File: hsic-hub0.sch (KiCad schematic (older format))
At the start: 17 parts

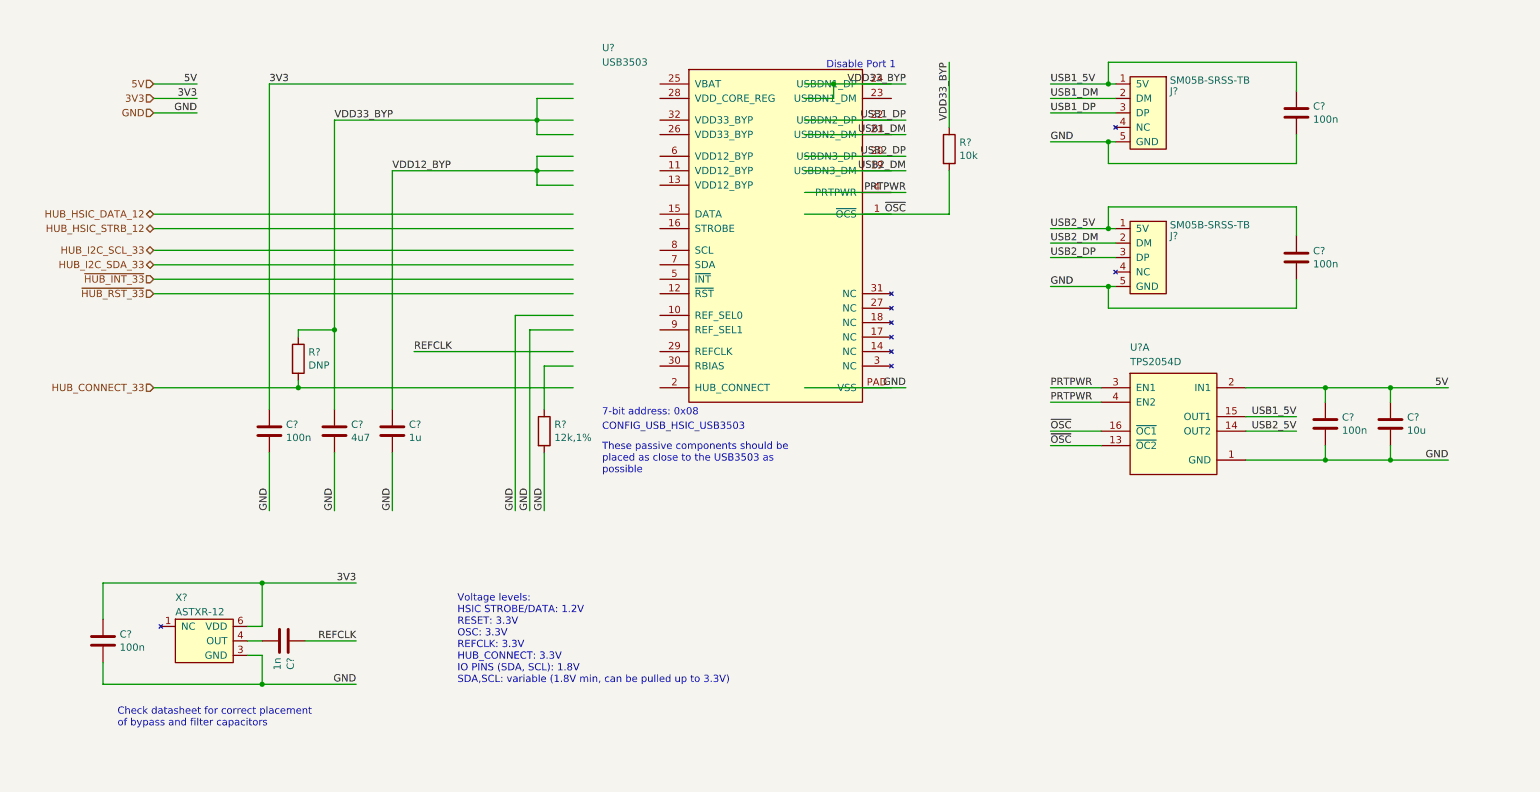
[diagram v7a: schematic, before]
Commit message: Major commit.
1. Fixed errors in libraries
2. Annoted schematics
3. Imported board shape and components into Pcbnew
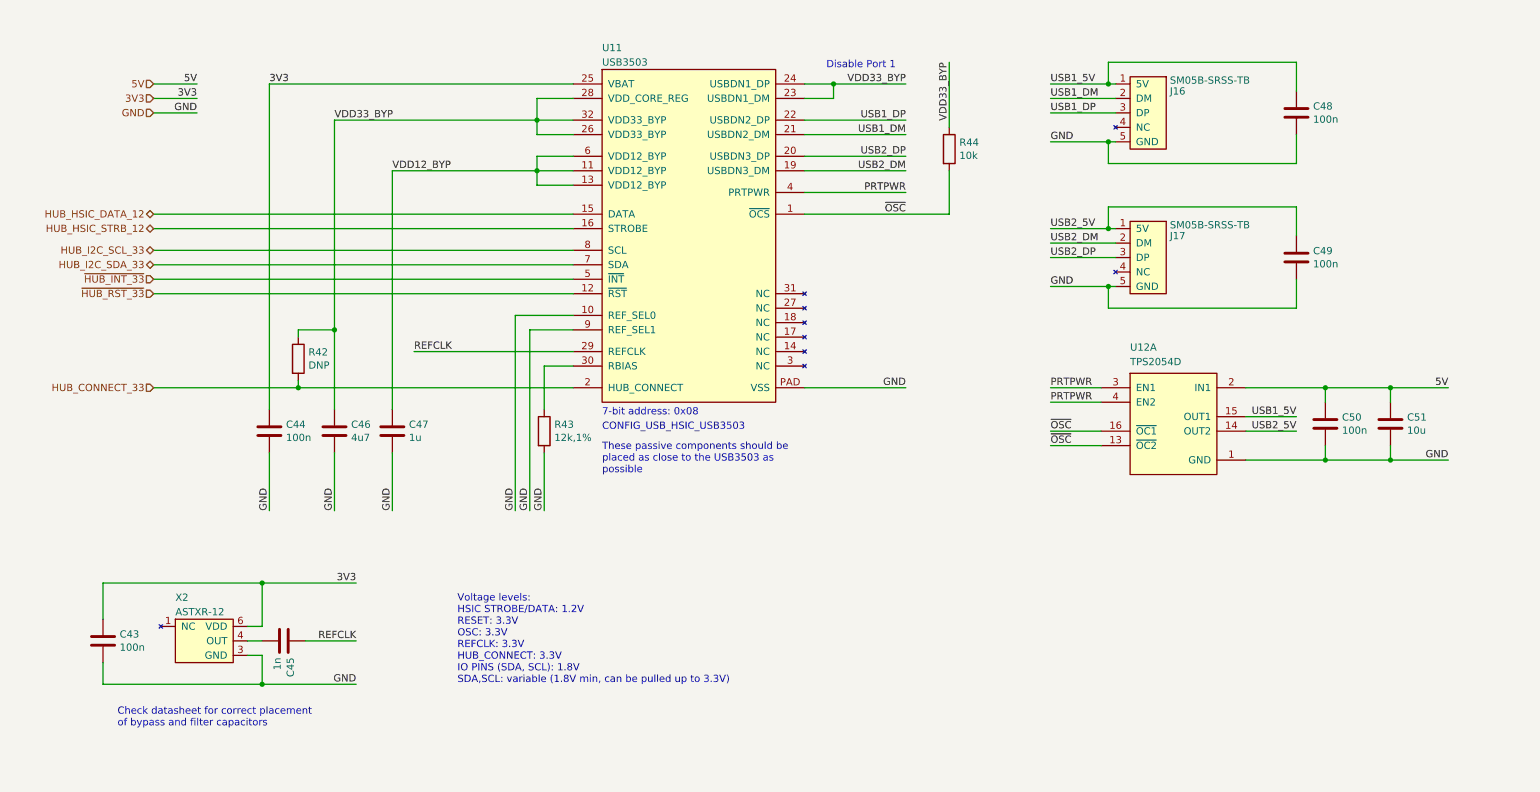
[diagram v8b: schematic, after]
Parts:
- removed C? (x2): 100n, Capacitor_SMD:C_0805_2012Metric_Pad1.15x1.40mm_HandSolder, symbol Drone:CAP
- removed C?: 1n, Capacitor_SMD:C_0805_2012Metric_Pad1.15x1.40mm_HandSolder, symbol Drone:CAP
- removed C?: 10u, Capacitor_SMD:C_0805_2012Metric_Pad1.15x1.40mm_HandSolder, symbol Drone:CAP
- removed R?: 12k,1%, Resistor_SMD:R_0805_2012Metric_Pad1.15x1.40mm_HandSolder, symbol Drone:RES
- removed X?: ASTXR-12, Drone:ASTXR-12, symbol Drone:ASTXR-12
- added C43, C48: 100n, Capacitor_SMD:C_0805_2012Metric, symbol Drone:CAP
- added C45: 1n, Capacitor_SMD:C_0805_2012Metric, symbol Drone:CAP
- added C51: 10u, Capacitor_SMD:C_0805_2012Metric, symbol Drone:CAP
- added R43: 12k,1%, Resistor_SMD:R_0805_2012Metric, symbol Drone:RES
- added X2: ASTXR-12, Drone:ASTXR-12, symbol Drone:ASTXR-12
- C44, C46, C47, C49, C50: renamed from C?; footprint Capacitor_SMD:C_0805_2012Metric_Pad1.15x1.40mm_HandSolder -> Capacitor_SMD:C_0805_2012Metric
- R42, R44: renamed from R?; footprint Resistor_SMD:R_0805_2012Metric_Pad1.15x1.40mm_HandSolder -> Resistor_SMD:R_0805_2012Metric
- U11: renamed from U?; footprint (none) -> Drone:USB3503ML
- gave numbers to parts that had none: 3
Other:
- moved on the sheet: U11
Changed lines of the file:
@@
 L Drone:USB3503 U?
 U 1 1 5E2F42C0
-P 5200 1050
+P 4600 1050
 AR Path="/5E2B9068/5E2F42C0" Ref="U?"  Part="1"
-AR Path="/5E2EDC4D/5E2F42C0" Ref="U?"  Part="1"
+AR Path="/5E2EDC4D/5E2F42C0" Ref="U11"  Part="1"
 AR Path="/5E349830/5E2F42C0" Ref="U?"  Part="1"
-F 0 "U?" H 4600 1200 50  0000 L CNN
+F 0 "U11" H 4600 1200 50  0000 L CNN
 F 1 "USB3503" H 4600 1100 50  0000 L CNN
-F 2 "" H 5200 1050 50  0001 C CNN
-F 3 "http://www.microchip.com/mymicrochip/filehandler.aspx?ddocname=en566511" H 5200 1050 50  0001 C CNN
-	1    5200 1050
+F 2 "Drone:USB3503ML" H 4600 1050 50  0001 C CNN
+F 3 "http://www.microchip.com/mymicrochip/filehandler.aspx?ddocname=en566511" H 4600 1050 50  0001 C CNN
+	1    4600 1050
 	1    0    0    -1
 $EndComp
@@
 	1500 2500 4400 2500
 $Comp
-L Drone:CAP C?
-U 1 1 5E328065
+L Drone:CAP C43
+U 1 1 5E888D19
 P 1150 5000
-AR Path="/5E2EDC4D/5E328065" Ref="C?"  Part="1"
-AR Path="/5E349830/5E328065" Ref="C?"  Part="1"
-F 0 "C?" H 1265 5046 50  0000 L CNN
+AR Path="/5E2EDC4D/5E888D19" Ref="C43"  Part="1"
+AR Path="/5E349830/5E888D19" Ref="C?"  Part="1"
+F 0 "C43" H 1265 5046 50  0000 L CNN
 F 1 "100n" H 1265 4955 50  0000 L CNN
-F 2 "Capacitor_SMD:C_0805_2012Metric_Pad1.15x1.40mm_HandSolder" H 1188 4850 50  0001 C CNN
+F 2 "Capacitor_SMD:C_0805_2012Metric" H 1188 4850 50  0001 C CNN
 F 3 "~" H 1150 5000 50  0001 C CNN
 	1    1150 5000
@@
 	6000 1900 6700 1900
 $Comp
-L Drone:CAP C?
+L Drone:CAP C50
 U 1 1 5E332CF8
 P 9600 3500
-AR Path="/5E2EDC4D/5E332CF8" Ref="C?"  Part="1"
+AR Path="/5E2EDC4D/5E332CF8" Ref="C50"  Part="1"
 AR Path="/5E349830/5E332CF8" Ref="C?"  Part="1"
-F 0 "C?" H 9715 3546 50  0000 L CNN
+F 0 "C50" H 9715 3546 50  0000 L CNN
 F 1 "100n" H 9715 3455 50  0000 L CNN
-F 2 "Capacitor_SMD:C_0805_2012Metric_Pad1.15x1.40mm_HandSolder" H 9638 3350 50  0001 C CNN
+F 2 "Capacitor_SMD:C_0805_2012Metric" H 9638 3350 50  0001 C CNN
 F 3 "~" H 9600 3500 50  0001 C CNN
 	1    9600 3500
@@
 GND
 $Comp
-L Drone:ASTXR-12 X?
-U 1 1 5E308236
+L Drone:ASTXR-12 X2
+U 1 1 5E888D18
 P 1850 4850
-AR Path="/5E2EDC4D/5E308236" Ref="X?"  Part="1"
-AR Path="/5E349830/5E308236" Ref="X?"  Part="1"
-F 0 "X?" H 1650 5000 50  0000 L CNN
+AR Path="/5E2EDC4D/5E888D18" Ref="X2"  Part="1"
+AR Path="/5E349830/5E888D18" Ref="X?"  Part="1"
+AR Path="/5E888D18" Ref="X2"  Part="1"
+F 0 "X2" H 1650 5000 50  0000 L CNN
 F 1 "ASTXR-12" H 1650 4900 50  0000 L CNN
 F 2 "Drone:ASTXR-12" H 1650 4500 50  0001 L CNN
@@
 	4000 2750 4400 2750
 $Comp
-L Drone:CAP C?
-U 1 1 5E338829
+L Drone:CAP C45
+U 1 1 5E888D1C
 P 2400 5000
-AR Path="/5E2EDC4D/5E338829" Ref="C?"  Part="1"
-AR Path="/5E349830/5E338829" Ref="C?"  Part="1"
-F 0 "C?" H 2515 5046 50  0000 L CNN
+AR Path="/5E2EDC4D/5E888D1C" Ref="C45"  Part="1"
+AR Path="/5E349830/5E888D1C" Ref="C?"  Part="1"
+F 0 "C45" H 2515 5046 50  0000 L CNN
 F 1 "1n" H 2515 4955 50  0000 L CNN
-F 2 "Capacitor_SMD:C_0805_2012Metric_Pad1.15x1.40mm_HandSolder" H 2438 4850 50  0001 C CNN
+F 2 "Capacitor_SMD:C_0805_2012Metric" H 2438 4850 50  0001 C CNN
 F 3 "~" H 2400 5000 50  0001 C CNN
 	1    2400 5000
@@
 Disable Port 1
 $Comp
-L Drone:CAP C?
-U 1 1 5E3408C5
+L Drone:CAP C48
+U 1 1 5E888D1D
 P 9400 1350
-AR Path="/5E2EDC4D/5E3408C5" Ref="C?"  Part="1"
-AR Path="/5E349830/5E3408C5" Ref="C?"  Part="1"
-F 0 "C?" H 9515 1396 50  0000 L CNN
+AR Path="/5E2EDC4D/5E888D1D" Ref="C48"  Part="1"
+AR Path="/5E349830/5E888D1D" Ref="C?"  Part="1"
+F 0 "C48" H 9515 1396 50  0000 L CNN
 F 1 "100n" H 9515 1305 50  0000 L CNN
-F 2 "Capacitor_SMD:C_0805_2012Metric_Pad1.15x1.40mm_HandSolder" H 9438 1200 50  0001 C CNN
+F 2 "Capacitor_SMD:C_0805_2012Metric" H 9438 1200 50  0001 C CNN
 F 3 "~" H 9400 1350 50  0001 C CNN
 	1    9400 1350
@@
 	8100 1550 8150 1550
 $Comp
-L Drone:CAP C?
+L Drone:CAP C49
 U 1 1 5E3AC9C8
 P 9400 2350
-AR Path="/5E2EDC4D/5E3AC9C8" Ref="C?"  Part="1"
+AR Path="/5E2EDC4D/5E3AC9C8" Ref="C49"  Part="1"
 AR Path="/5E349830/5E3AC9C8" Ref="C?"  Part="1"
-F 0 "C?" H 9515 2396 50  0000 L CNN
+F 0 "C49" H 9515 2396 50  0000 L CNN
 F 1 "100n" H 9515 2305 50  0000 L CNN
-F 2 "Capacitor_SMD:C_0805_2012Metric_Pad1.15x1.40mm_HandSolder" H 9438 2200 50  0001 C CNN
+F 2 "Capacitor_SMD:C_0805_2012Metric" H 9438 2200 50  0001 C CNN
 F 3 "~" H 9400 2350 50  0001 C CNN
 	1    9400 2350
@@
 ~OSC
 $Comp
-L Drone:TPS2054D U?
+L Drone:TPS2054D U12
 U 1 1 5E4E09E8
 P 8550 3150
-AR Path="/5E2EDC4D/5E4E09E8" Ref="U?"  Part="1"
+AR Path="/5E2EDC4D/5E4E09E8" Ref="U12"  Part="1"
 AR Path="/5E349830/5E4E09E8" Ref="U?"  Part="1"
-F 0 "U?" H 8250 3300 50  0000 L BNN
+F 0 "U12" H 8250 3300 50  0000 L BNN
 F 1 "TPS2054D" H 8250 3200 50  0000 L BNN
 F 2 "Package_SO:SOIC-16_3.9x9.9mm_P1.27mm" H 8250 3400 50  0001 L BNN
@@
 	6000 2050 7000 2050
 $Comp
-L Drone:RES R?
+L Drone:RES R44
 U 1 1 5E301315
 P 7000 1600
-AR Path="/5E2EDC4D/5E301315" Ref="R?"  Part="1"
+AR Path="/5E2EDC4D/5E301315" Ref="R44"  Part="1"
 AR Path="/5E349830/5E301315" Ref="R?"  Part="1"
-F 0 "R?" H 7070 1646 50  0000 L CNN
+F 0 "R44" H 7070 1646 50  0000 L CNN
 F 1 "10k" H 7070 1555 50  0000 L CNN
-F 2 "Resistor_SMD:R_0805_2012Metric_Pad1.15x1.40mm_HandSolder" V 6930 1600 50  0001 C CNN
+F 2 "Resistor_SMD:R_0805_2012Metric" V 6930 1600 50  0001 C CNN
 F 3 "~" H 7000 1600 50  0001 C CNN
 	1    7000 1600
@@
 	7000 2050 7000 1750
 $Comp
-L Drone:SM05B-SRSS-TB J?
+L Drone:SM05B-SRSS-TB J16
 U 1 1 5E385FFC
 P 8500 1100
-AR Path="/5E2EDC4D/5E385FFC" Ref="J?"  Part="1"
+AR Path="/5E2EDC4D/5E385FFC" Ref="J16"  Part="1"
 AR Path="/5E349830/5E385FFC" Ref="J?"  Part="1"
-F 0 "J?" H 8475 1000 50  0000 R CNN
+F 0 "J16" H 8475 1000 50  0000 R CNN
 F 1 "SM05B-SRSS-TB" H 8475 1075 50  0000 R CNN
 F 2 "Drone:SM05B-SRSS-TB" H 8350 1350 50  0001 L CNN
@@
 $EndComp
 $Comp
-L Drone:SM05B-SRSS-TB J?
+L Drone:SM05B-SRSS-TB J17
 U 1 1 5E3AC9C2
 P 8500 2100
-AR Path="/5E2EDC4D/5E3AC9C2" Ref="J?"  Part="1"
+AR Path="/5E2EDC4D/5E3AC9C2" Ref="J17"  Part="1"
 AR Path="/5E349830/5E3AC9C2" Ref="J?"  Part="1"
-F 0 "J?" H 8475 2000 50  0000 R CNN
+F 0 "J17" H 8475 2000 50  0000 R CNN
 F 1 "SM05B-SRSS-TB" H 8475 2075 50  0000 R CNN
 F 2 "Drone:SM05B-SRSS-TB" H 8350 2350 50  0001 L CNN
@@
 $EndComp
 $Comp
-L Drone:CAP C?
-U 1 1 5E5A610D
+L Drone:CAP C51
+U 1 1 5E888D24
 P 10050 3500
-AR Path="/5E2EDC4D/5E5A610D" Ref="C?"  Part="1"
-AR Path="/5E349830/5E5A610D" Ref="C?"  Part="1"
-F 0 "C?" H 10165 3546 50  0000 L CNN
+AR Path="/5E2EDC4D/5E888D24" Ref="C51"  Part="1"
+AR Path="/5E349830/5E888D24" Ref="C?"  Part="1"
+F 0 "C51" H 10165 3546 50  0000 L CNN
 F 1 "10u" H 10165 3455 50  0000 L CNN
-F 2 "Capacitor_SMD:C_0805_2012Metric_Pad1.15x1.40mm_HandSolder" H 10088 3350 50  0001 C CNN
+F 2 "Capacitor_SMD:C_0805_2012Metric" H 10088 3350 50  0001 C CNN
 F 3 "~" H 10050 3500 50  0001 C CNN
 	1    10050 3500
@@
 These passive components should be\nplaced as close to the USB3503 as\npossible\n
 $Comp
-L Drone:CAP C?
+L Drone:CAP C46
 U 1 1 5E427B4C
 P 2750 3550
-AR Path="/5E2EDC4D/5E427B4C" Ref="C?"  Part="1"
+AR Path="/5E2EDC4D/5E427B4C" Ref="C46"  Part="1"
 AR Path="/5E349830/5E427B4C" Ref="C?"  Part="1"
-F 0 "C?" H 2865 3596 50  0000 L CNN
+F 0 "C46" H 2865 3596 50  0000 L CNN
 F 1 "4u7" H 2865 3505 50  0000 L CNN
-F 2 "Capacitor_SMD:C_0805_2012Metric_Pad1.15x1.40mm_HandSolder" H 2788 3400 50  0001 C CNN
+F 2 "Capacitor_SMD:C_0805_2012Metric" H 2788 3400 50  0001 C CNN
 F 3 "~" H 2750 3550 50  0001 C CNN
 	1    2750 3550
@@
 $EndComp
 $Comp
-L Drone:CAP C?
+L Drone:CAP C47
 U 1 1 5E42226D
 P 3150 3550
-AR Path="/5E2EDC4D/5E42226D" Ref="C?"  Part="1"
+AR Path="/5E2EDC4D/5E42226D" Ref="C47"  Part="1"
 AR Path="/5E349830/5E42226D" Ref="C?"  Part="1"
-F 0 "C?" H 3265 3596 50  0000 L CNN
+F 0 "C47" H 3265 3596 50  0000 L CNN
 F 1 "1u" H 3265 3505 50  0000 L CNN
-F 2 "Capacitor_SMD:C_0805_2012Metric_Pad1.15x1.40mm_HandSolder" H 3188 3400 50  0001 C CNN
+F 2 "Capacitor_SMD:C_0805_2012Metric" H 3188 3400 50  0001 C CNN
 F 3 "~" H 3150 3550 50  0001 C CNN
 	1    3150 3550
@@
 	4100 4100 4100 2850
 $Comp
-L Drone:RES R?
-U 1 1 5E32A1DA
+L Drone:RES R43
+U 1 1 5E888D1A
 P 4200 3550
-AR Path="/5E2EDC4D/5E32A1DA" Ref="R?"  Part="1"
-AR Path="/5E349830/5E32A1DA" Ref="R?"  Part="1"
-F 0 "R?" H 4270 3596 50  0000 L CNN
+AR Path="/5E2EDC4D/5E888D1A" Ref="R43"  Part="1"
+AR Path="/5E349830/5E888D1A" Ref="R?"  Part="1"
+F 0 "R43" H 4270 3596 50  0000 L CNN
 F 1 "12k,1%" H 4270 3505 50  0000 L CNN
-F 2 "Resistor_SMD:R_0805_2012Metric_Pad1.15x1.40mm_HandSolder" V 4130 3550 50  0001 C CNN
+F 2 "Resistor_SMD:R_0805_2012Metric" V 4130 3550 50  0001 C CNN
 F 3 "~" H 4200 3550 50  0001 C CNN
 	1    4200 3550
@@
 7-bit address: 0x08
 $Comp
-L Drone:RES R?
+L Drone:RES R42
 U 1 1 5E6510FD
 P 2500 3050
-AR Path="/5E2EDC4D/5E6510FD" Ref="R?"  Part="1"
+AR Path="/5E2EDC4D/5E6510FD" Ref="R42"  Part="1"
 AR Path="/5E349830/5E6510FD" Ref="R?"  Part="1"
-F 0 "R?" H 2570 3096 50  0000 L CNN
+F 0 "R42" H 2570 3096 50  0000 L CNN
 F 1 "DNP" H 2570 3005 50  0000 L CNN
-F 2 "Resistor_SMD:R_0805_2012Metric_Pad1.15x1.40mm_HandSolder" V 2430 3050 50  0001 C CNN
+F 2 "Resistor_SMD:R_0805_2012Metric" V 2430 3050 50  0001 C CNN
 F 3 "~" H 2500 3050 50  0001 C CNN
 	1    2500 3050
@@
 	2300 1150 4400 1150
 $Comp
-L Drone:CAP C?
+L Drone:CAP C44
 U 1 1 5E74B35F
 P 2300 3550
-AR Path="/5E2EDC4D/5E74B35F" Ref="C?"  Part="1"
+AR Path="/5E2EDC4D/5E74B35F" Ref="C44"  Part="1"
 AR Path="/5E349830/5E74B35F" Ref="C?"  Part="1"
-F 0 "C?" H 2415 3596 50  0000 L CNN
+F 0 "C44" H 2415 3596 50  0000 L CNN
 F 1 "100n" H 2415 3505 50  0000 L CNN
-F 2 "Capacitor_SMD:C_0805_2012Metric_Pad1.15x1.40mm_HandSolder" H 2338 3400 50  0001 C CNN
+F 2 "Capacitor_SMD:C_0805_2012Metric" H 2338 3400 50  0001 C CNN
 F 3 "~" H 2300 3550 50  0001 C CNN
 	1    2300 3550
